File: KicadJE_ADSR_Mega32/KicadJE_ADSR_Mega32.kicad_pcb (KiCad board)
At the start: 2 copper layers, 100 x 100 mm, 100 parts, among them J101 In, J102 Out, J201 AVR-ISP-6, J202 UART, J301 In, J302 +5V reg/doepfer, J303 Out, J304 CV_time, J305 CV doepfer, P101 Doepfer_Power_16pin, P302 Doepfer_Power_16pin, Q301 BC337, Q302 PZT2222A, U201 ATmega32A-AU, U301 L78L05_TO92, U302 PT2399, Y201 16MHz

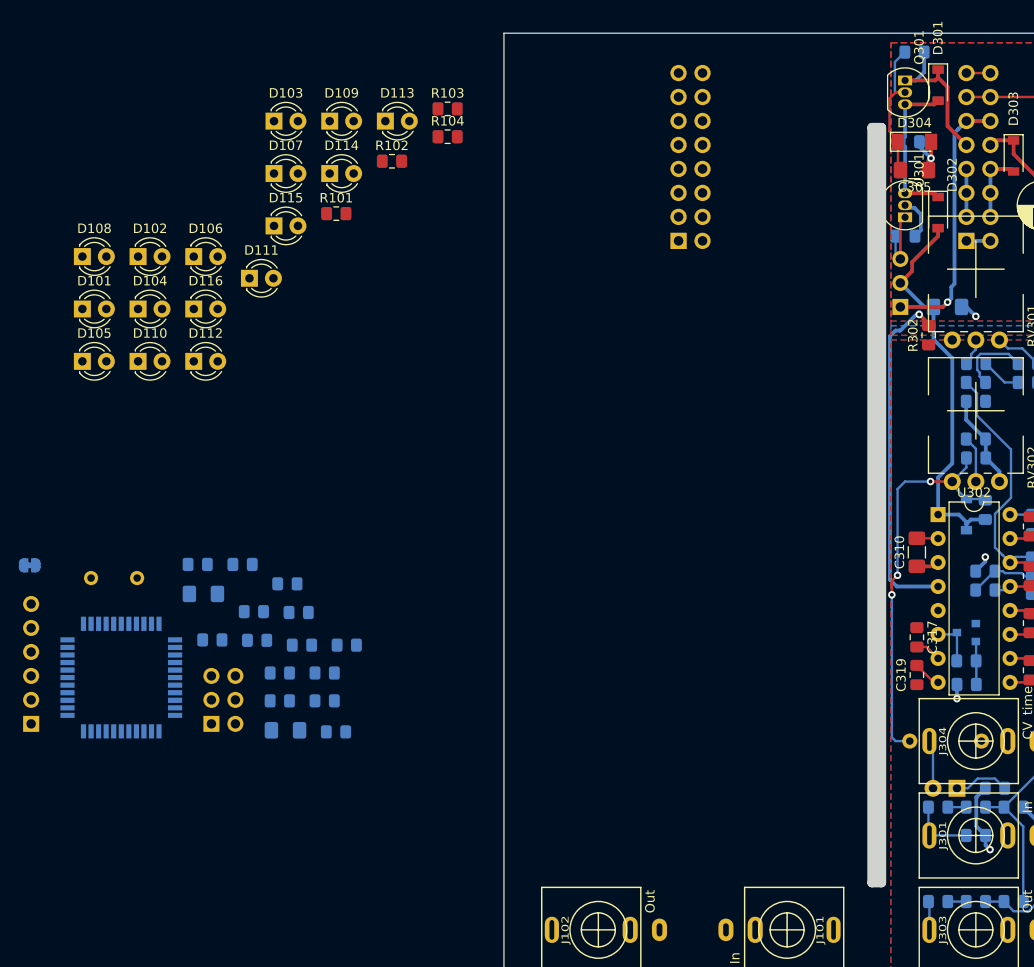
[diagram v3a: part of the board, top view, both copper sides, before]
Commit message: Change LED Matrix pins
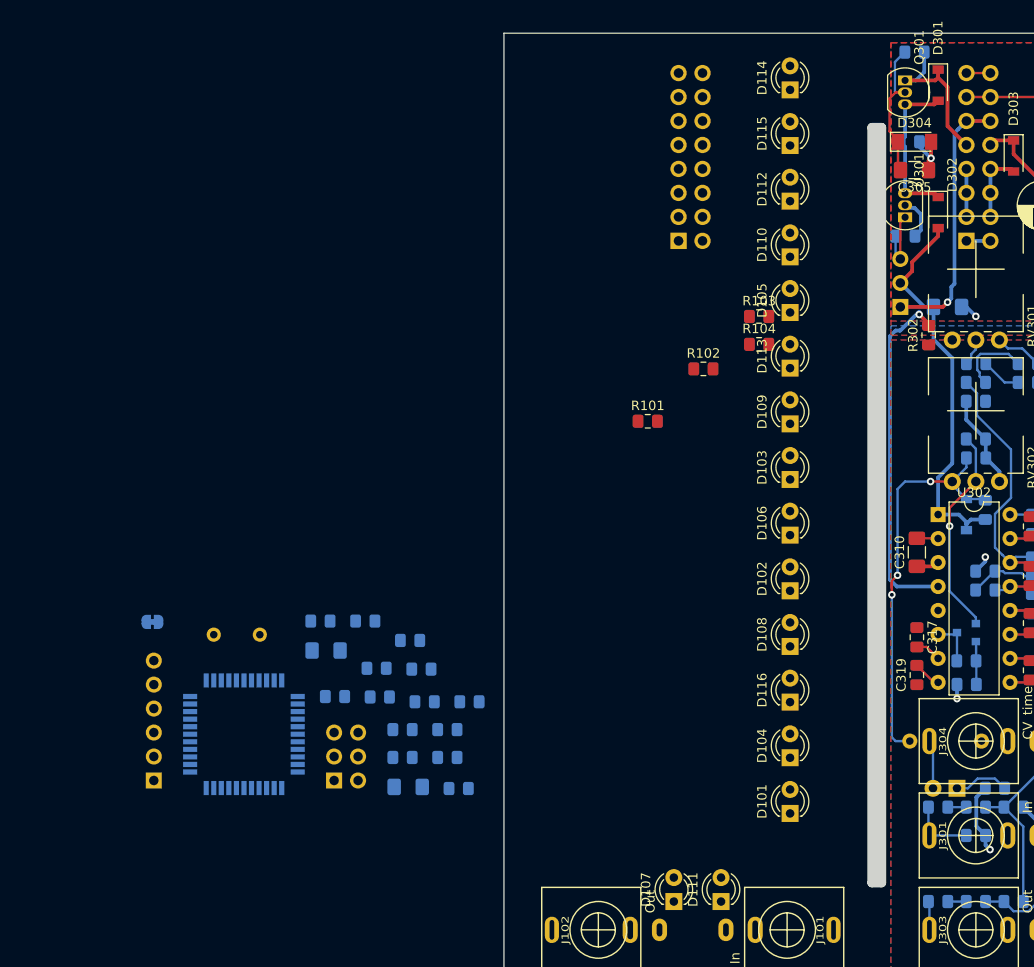
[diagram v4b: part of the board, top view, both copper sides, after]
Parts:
- moved D101 92.1 mm to (80.3, 132.7), turned to 90 degrees
- moved D107 88.0 mm to (68.0, 142.0), turned to 90 degrees
- moved D108 85.6 mm to (80.3, 115.0), turned to 90 degrees
- moved D104 83.9 mm to (80.3, 126.8), turned to 90 degrees
- moved D111 82.8 mm to (73.0, 142.0), turned to 90 degrees
- moved D102 77.6 mm to (80.3, 109.1), turned to 90 degrees
- moved D116 75.7 mm to (80.3, 120.9), turned to 90 degrees
- moved D105 75.2 mm to (80.3, 79.6), turned to 90 degrees
- moved D110 70.0 mm to (80.3, 73.7), turned to 90 degrees
- moved D106 69.7 mm to (80.3, 103.2), turned to 90 degrees
- moved D103 66.6 mm to (80.3, 97.3), turned to 90 degrees
- moved D112 65.4 mm to (80.3, 67.8), turned to 90 degrees
- moved D109 58.4 mm to (80.3, 91.4), turned to 90 degrees
- moved D115 55.3 mm to (80.3, 61.9), turned to 90 degrees
- moved D113 50.2 mm to (80.3, 85.5), turned to 90 degrees
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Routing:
- net Net-(C321-Pad2): track 4.92 -> 22.3 mm, vias 0 -> 1

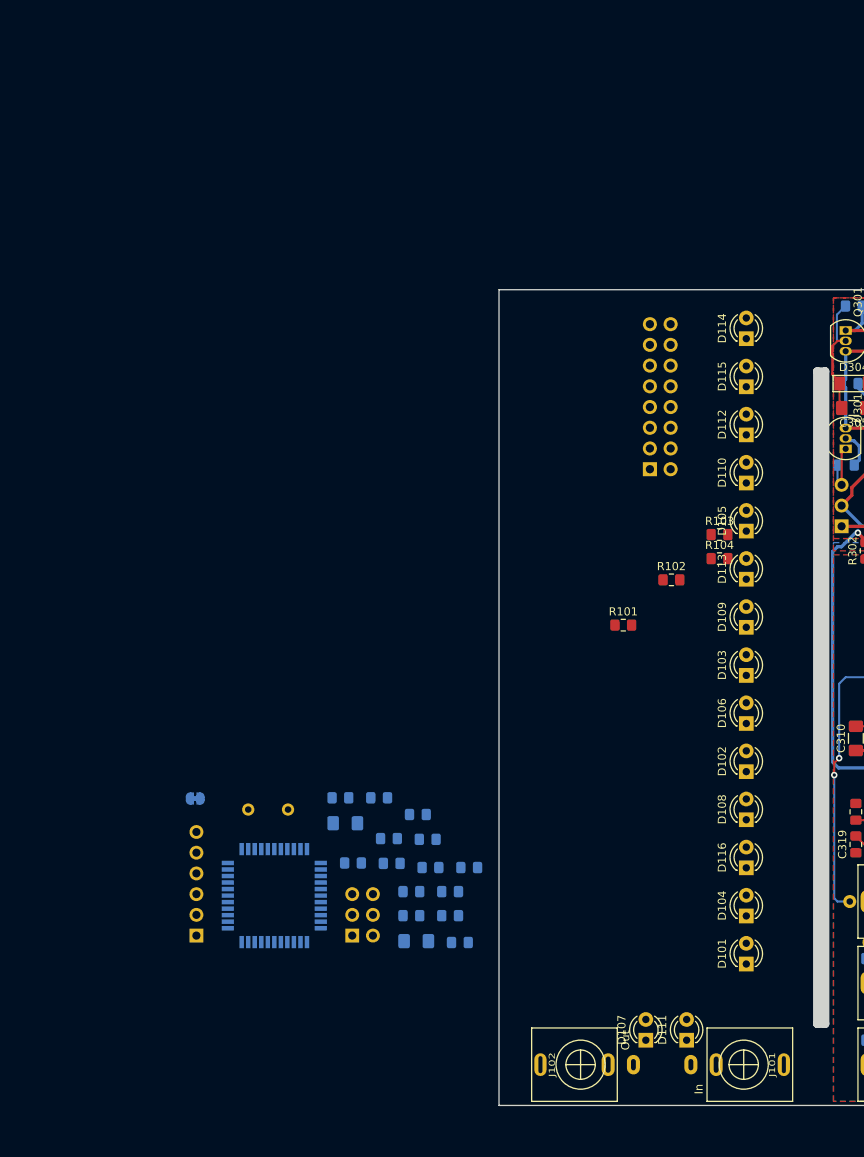
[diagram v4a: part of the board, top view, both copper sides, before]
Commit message: Reduce to 8pot and 8jack
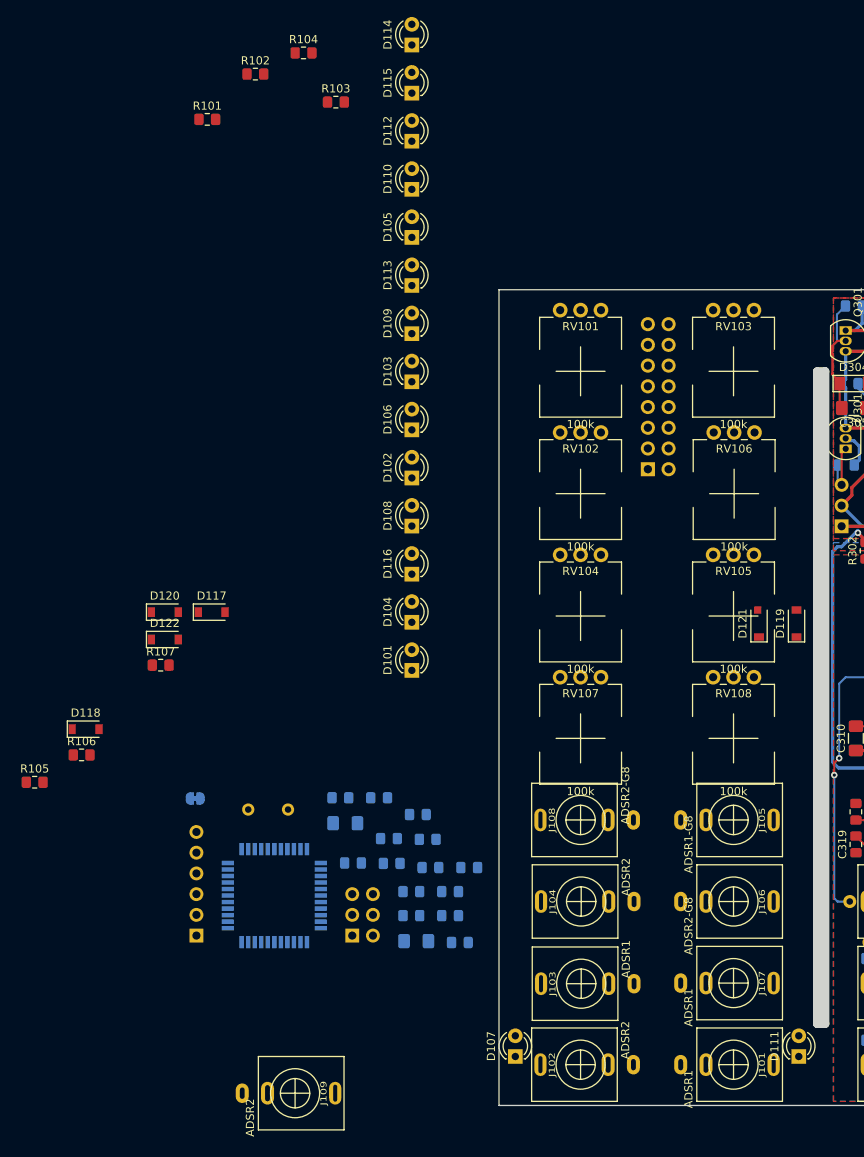
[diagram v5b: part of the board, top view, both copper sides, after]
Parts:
- added D117: 1N1007, Diode_SMD:D_SOD-123, F.Cu at (14.8, 89.5)
- added D118: 1N1007, Diode_SMD:D_SOD-123, F.Cu at (-0.67, 103.9)
- added D119: 1N1007, Diode_SMD:D_SOD-123, F.Cu at (86.5, 90.9)
- added D120: 1N1007, Diode_SMD:D_SOD-123, F.Cu at (9.03, 89.5)
- added D121: 1N1007, Diode_SMD:D_SOD-123, F.Cu at (81.9, 90.9)
- added D122: 1N1007, Diode_SMD:D_SOD-123, F.Cu at (9.03, 92.9)
- added J103: ADSR1, AJ-Dropbox-Kicad:PJ301SM, F.Cu at (60.1, 135.1)
- added J104: ADSR2, AJ-Dropbox-Kicad:PJ301SM, F.Cu at (60.1, 125.0)
- added J105: ADSR1-G8, AJ-Dropbox-Kicad:PJ301SM, F.Cu at (78.8, 115.0)
- added J106: ADSR2-G8, AJ-Dropbox-Kicad:PJ301SM, F.Cu at (78.8, 125.0)
- added J107: ADSR1, AJ-Dropbox-Kicad:PJ301SM, F.Cu at (78.8, 135.0)
- added J108: ADSR2-G8, AJ-Dropbox-Kicad:PJ301SM, F.Cu at (60.0, 115.0)
- added J109: ADSR2, AJ-Dropbox-Kicad:PJ301SM, F.Cu at (25.0, 148.5)
- added R105: 10k, Resistor_SMD:R_0805_2012Metric_Pad1.15x1.40mm_HandSolder, F.Cu at (-6.92, 110.4)
- added R106: 10k, Resistor_SMD:R_0805_2012Metric_Pad1.15x1.40mm_HandSolder, F.Cu at (-1.17, 107.0)
- added R107: 10k, Resistor_SMD:R_0805_2012Metric_Pad1.15x1.40mm_HandSolder, F.Cu at (8.53, 96.0)
- added RV101: 100k, Potentiometer_THT:Potentiometer_China_RK09_Single_Vertical_AJ, F.Cu at (57.5, 52.5)
- added RV102: 100k, Potentiometer_THT:Potentiometer_China_RK09_Single_Vertical_AJ, F.Cu at (57.5, 67.5)
- added RV103: 100k, Potentiometer_THT:Potentiometer_China_RK09_Single_Vertical_AJ, F.Cu at (76.2, 52.5)
- added RV104: 100k, Potentiometer_THT:Potentiometer_China_RK09_Single_Vertical_AJ, F.Cu at (57.5, 82.5)
- added RV105: 100k, Potentiometer_THT:Potentiometer_China_RK09_Single_Vertical_AJ, F.Cu at (76.2, 82.5)
- added RV106: 100k, Potentiometer_THT:Potentiometer_China_RK09_Single_Vertical_AJ, F.Cu at (76.3, 67.5)
- added RV107: 100k, Potentiometer_THT:Potentiometer_China_RK09_Single_Vertical_AJ, F.Cu at (57.5, 97.5)
- added RV108: 100k, Potentiometer_THT:Potentiometer_China_RK09_Single_Vertical_AJ, F.Cu at (76.2, 97.5)
- J101: value In -> ADSR1
- J102: value Out -> ADSR2
- moved R102 80.3 mm to (20.1, 23.6)
- moved R101 80.3 mm to (14.2, 29.1)
- moved R104 80.3 mm to (26.0, 21.0)
- moved R103 70.9 mm to (30.0, 27.0)
- moved D101 54.6 mm to (39.3, 96.7)
- moved D102 54.6 mm to (39.3, 73.1)
- moved D103 54.6 mm to (39.3, 61.3)
- moved D104 54.6 mm to (39.3, 90.8)
- moved D105 54.6 mm to (39.3, 43.6)
- moved D106 54.6 mm to (39.3, 67.2)
- moved D108 54.6 mm to (39.3, 79.0)
- moved D109 54.6 mm to (39.3, 55.4)
- moved D110 54.6 mm to (39.3, 37.7)
- moved D112 54.6 mm to (39.3, 31.8)
- moved D113 54.6 mm to (39.3, 49.5)
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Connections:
- D101 pad 2: 0_LED -> 18
- D105 pad 2: 1 -> 19
- D109 pad 2: 2_INT2 -> 20
- D113 pad 2: 3_PWM -> 21
- J101 pad T: (no net) -> 3_PWM
- J102 pad T: (no net) -> 4_PWM
- R101 pad 1: 4_PWM -> 22
- R102 pad 1: 5_MOSI -> 23
- R103 pad 1: 6_MISO -> 1
- R104 pad 1: 7_SCK -> 0_LED
- U201 pad 11: (no net) -> 10_INT0
- U201 pad 12: (no net) -> 11_INT1
- U201 pad 13: (no net) -> 12_PWM
- U201 pad 14: (no net) -> 13_PWM
- U201 pad 15: (no net) -> 14_PWM
- U201 pad 16: (no net) -> 15_PWM
- U201 pad 21: (no net) -> 18
- U201 pad 22: (no net) -> 19
- U201 pad 23: (no net) -> 20
- U201 pad 24: (no net) -> 21
- U201 pad 25: (no net) -> 22
- U201 pad 26: (no net) -> 23
- U201 pad 30: (no net) -> 31_A7
- U201 pad 31: (no net) -> 30_A6
- U201 pad 32: (no net) -> 29_A5
- U201 pad 33: (no net) -> 28_A4
- U201 pad 34: (no net) -> 27_A3
- U201 pad 35: (no net) -> 26_A2
- U201 pad 36: (no net) -> 25_A1
- U201 pad 37: (no net) -> 24_A0

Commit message: PCB update
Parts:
- removed J109: ADSR2, AJ-Dropbox-Kicad:PJ301SM
- added D123: 1N1007, Diode_SMD:D_SOD-123, F.Cu at (81.9, 160.9)
- added D124: 1N1007, Diode_SMD:D_SOD-123, F.Cu at (81.9, 164.3)
- added R108: 10k, Resistor_SMD:R_0805_2012Metric_Pad1.15x1.40mm_HandSolder, F.Cu at (81.4, 167.4)
- added R109: 10k, Resistor_SMD:R_0805_2012Metric_Pad1.15x1.40mm_HandSolder, F.Cu at (81.4, 170.4)
- added R110: 10k, Resistor_SMD:R_0805_2012Metric_Pad1.15x1.40mm_HandSolder, F.Cu at (81.4, 173.3)
- J107: value ADSR1 -> ADSR4-G8
- J108: value ADSR2-G8 -> ADSR3-G8
- moved R105 89.5 mm to (48.8, 180.5)
- moved D108 76.5 mm to (87.1, 138.7)
- moved D117 75.8 mm to (51.5, 155.8)
- moved D118 75.8 mm to (36.1, 170.1)
- moved D120 75.8 mm to (45.8, 155.8)
- moved D122 75.8 mm to (45.8, 159.1)
- moved R106 75.8 mm to (35.6, 173.3)
- moved R107 75.8 mm to (45.3, 162.3)
- moved D102 73.4 mm to (87.1, 128.8)
- moved D119 73.2 mm to (72.2, 162.7)
- moved D121 73.2 mm to (67.6, 162.7)
- moved D106 70.3 mm to (87.1, 118.8)
- moved D101 43.8 mm to (51.6, 138.7)
- moved D105 41.1 mm to (44.6, 84.3)
- moved D103 41.1 mm to (44.6, 102.0)
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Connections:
- J101 pad T: 3_PWM -> ADSR1
- J101 pad TN: (no net) -> Net-(J101-PadTN)
- J107 pad T: 14_PWM -> (no net)
- J107 pad TN: (no net) -> Net-(J107-PadTN)
- U201 pad 15: 14_PWM -> (no net)
- U201 pad 16: 15_PWM -> (no net)

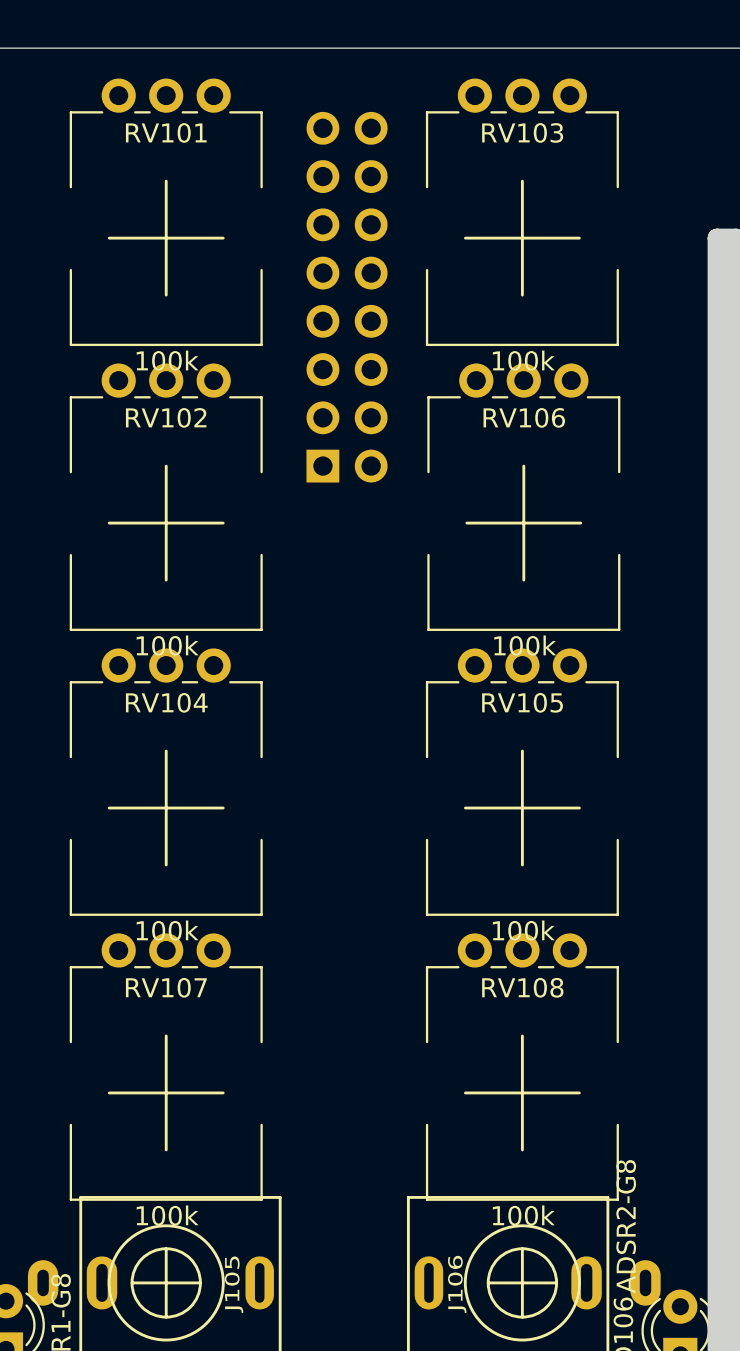
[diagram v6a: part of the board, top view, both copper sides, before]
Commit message: 6 pot and added LP for all PWM out
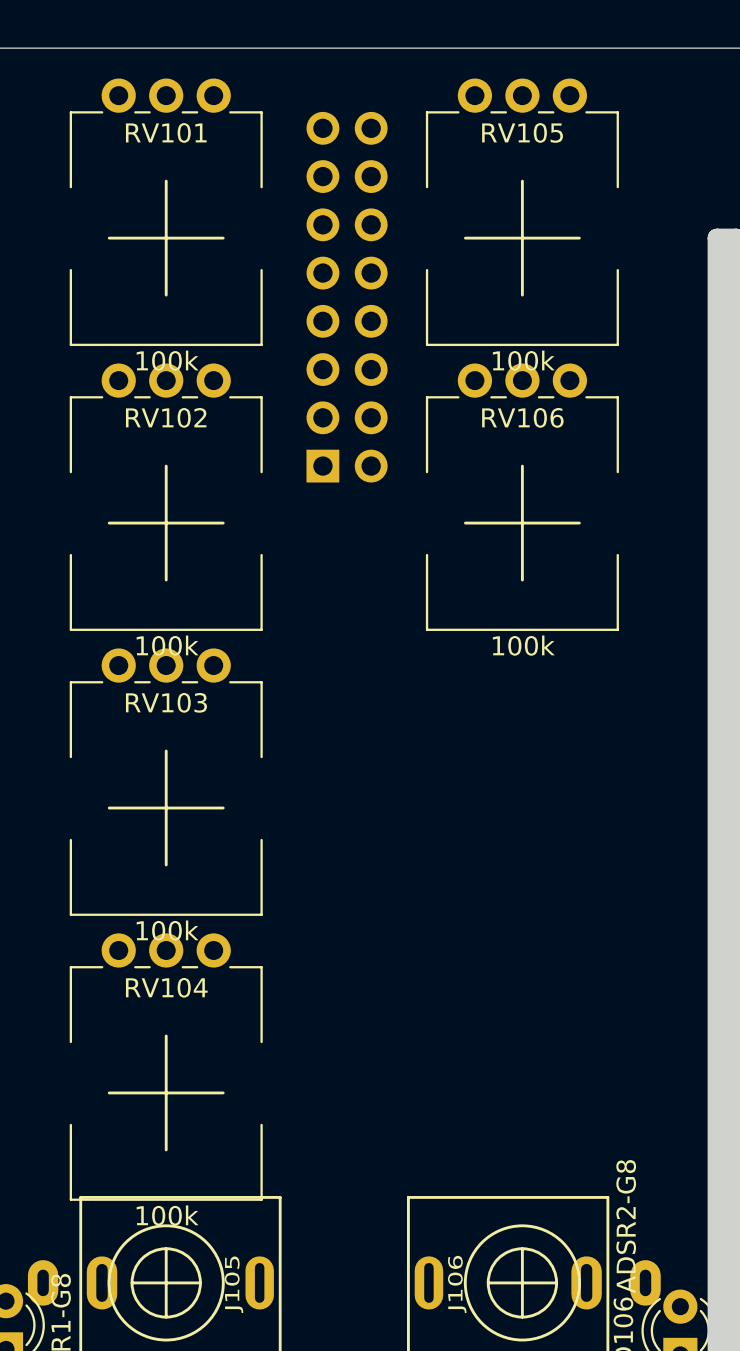
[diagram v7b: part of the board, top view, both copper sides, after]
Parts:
- removed RV107, RV108: 100k, Potentiometer_THT:Potentiometer_China_RK09_Single_Vertical_AJ
- moved RV103 35.4 mm to (57.5, 82.5)
- moved RV105 30.0 mm to (76.2, 52.5)
- moved RV104 15.0 mm to (57.5, 97.5)
- moved RV106 0.07 mm to (76.2, 67.5)
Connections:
- U201 pad 30: 31_A7 -> (no net)
- U201 pad 31: 30_A6 -> (no net)
